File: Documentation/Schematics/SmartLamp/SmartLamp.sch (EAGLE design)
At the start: 34 parts, among them J1 POWER_JACKPTH_BREAD, Q1 STN4NF03L, Q2 STN4NF03L, Q3 STN4NF03L, U1 TPS71530, U2 DS3231MZ, U3 ATMEGA8/168/328MLF, U4 HM-10, X1 16MHz

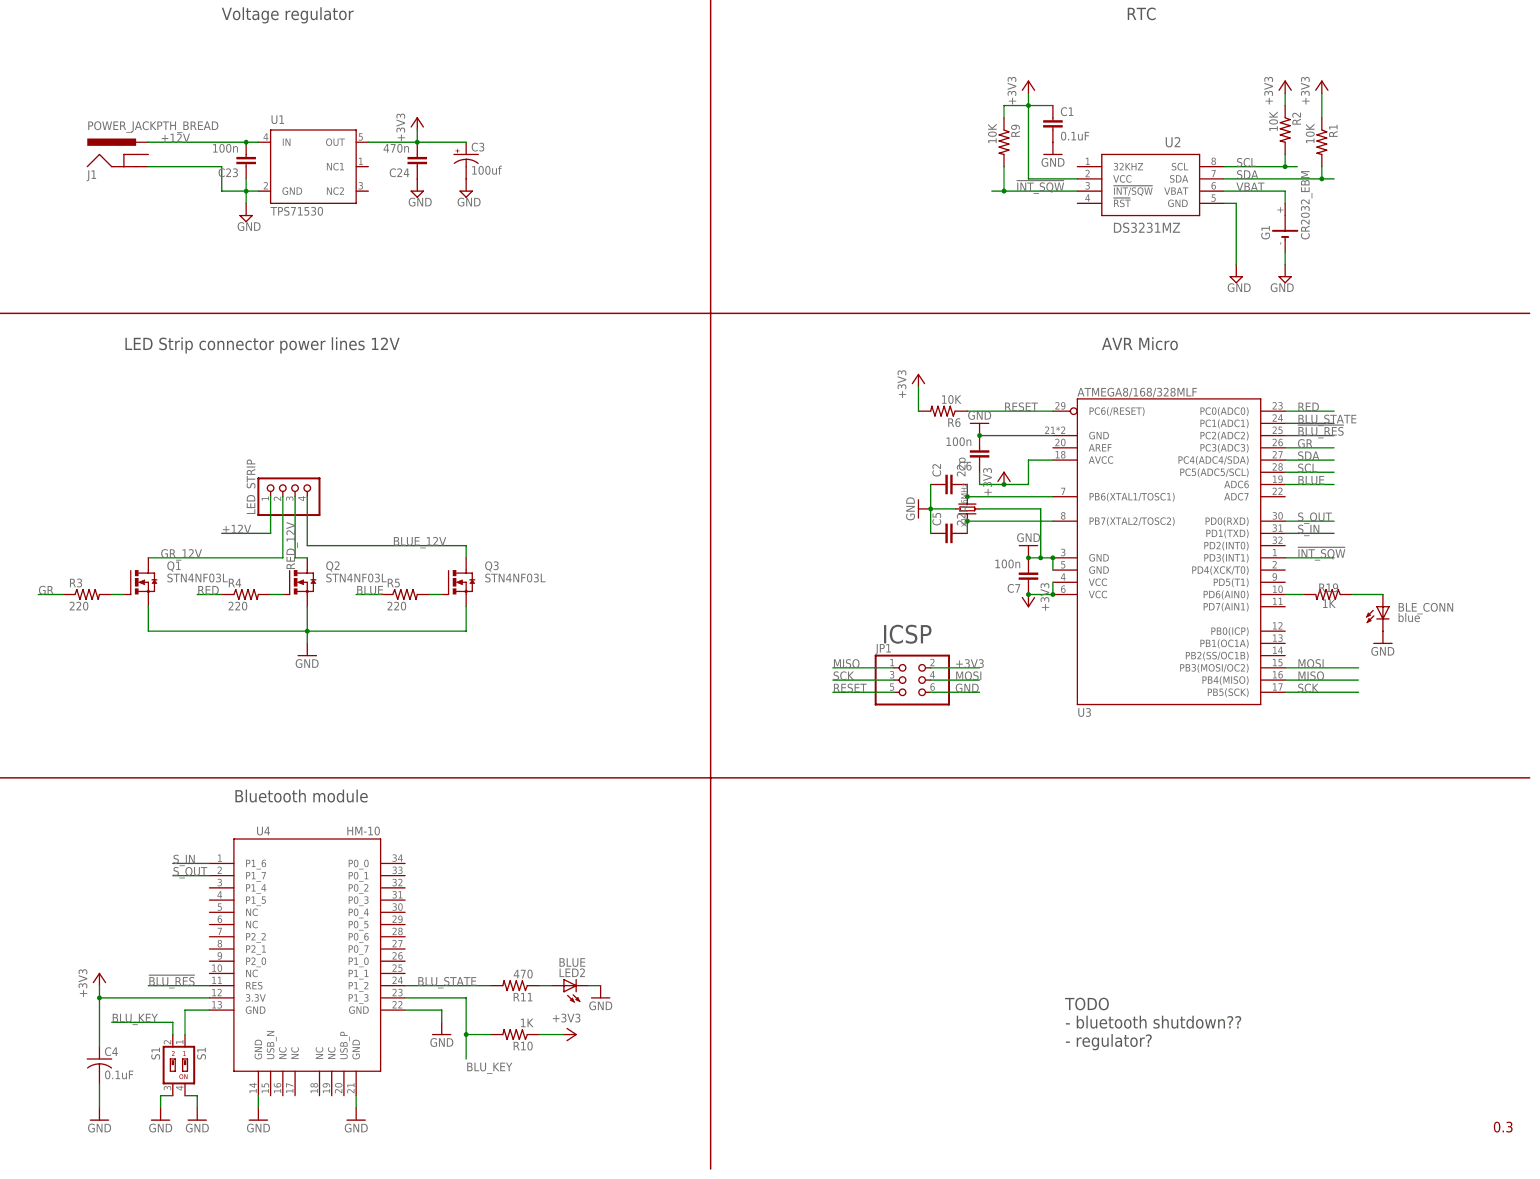
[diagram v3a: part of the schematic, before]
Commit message: Changed micro package, added IDC connector, replace regulatot. Some component to be checked
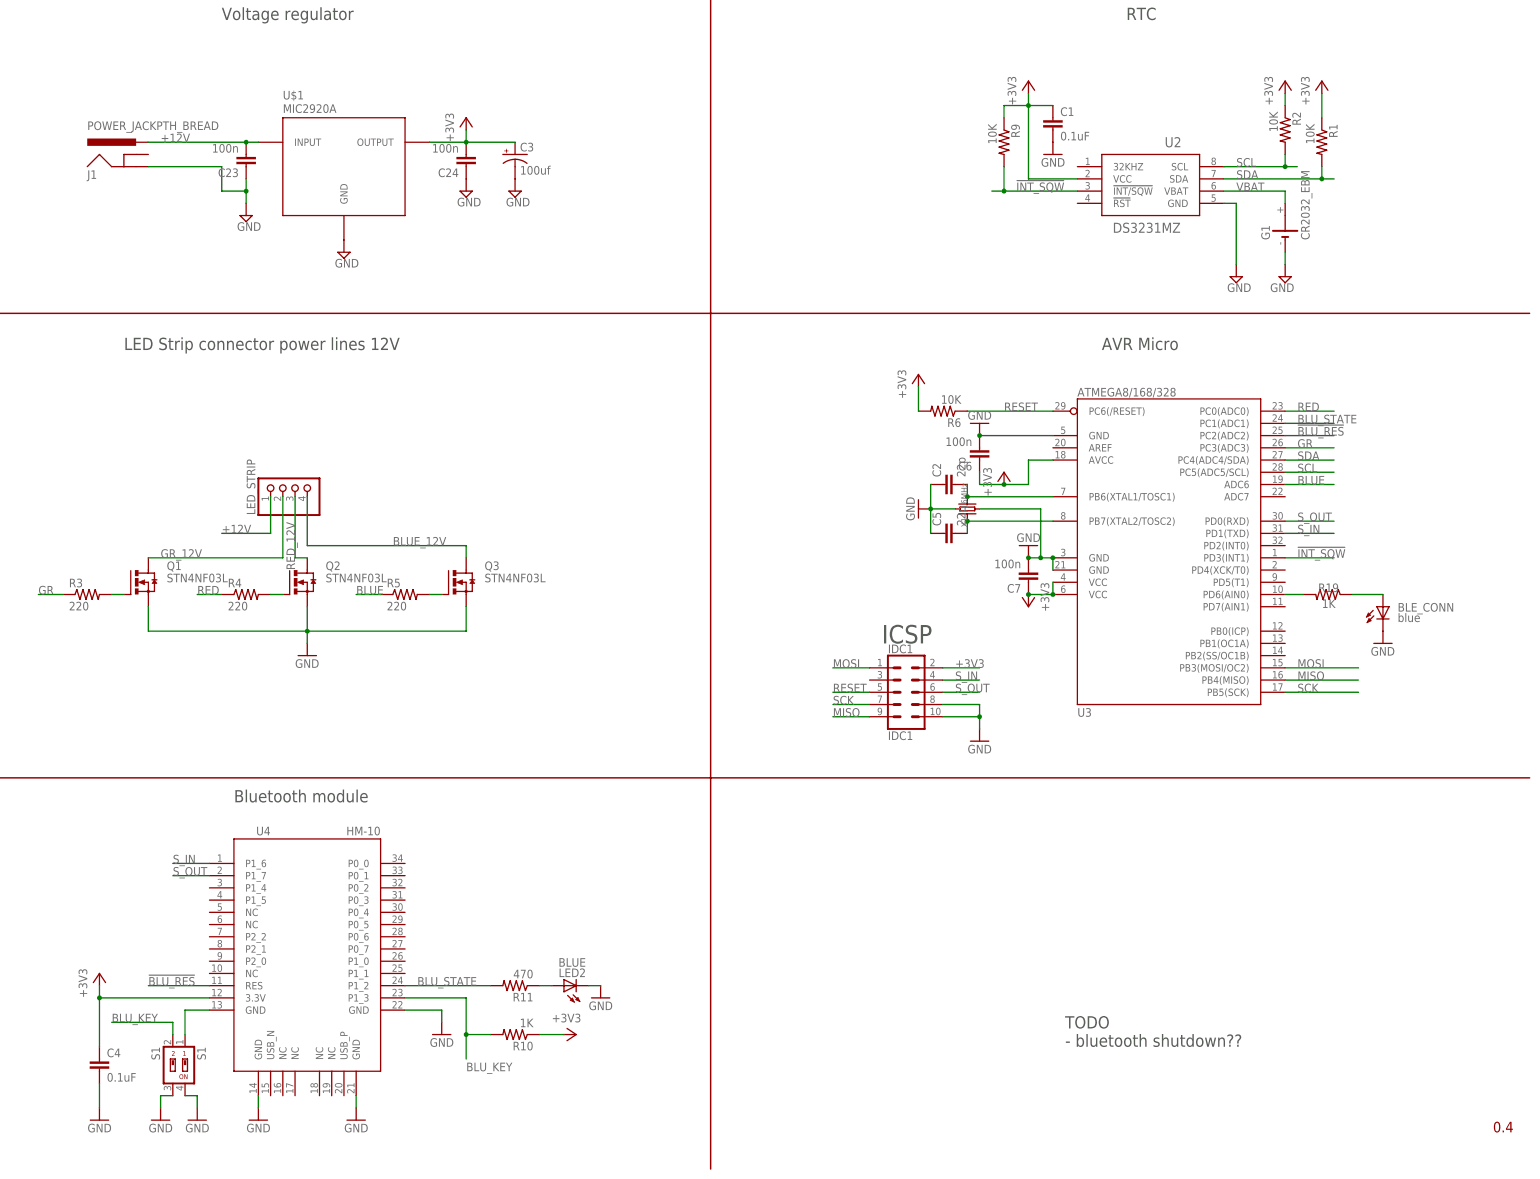
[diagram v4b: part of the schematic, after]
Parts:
- removed JP1: (no value), pinhead:PINHD-2X3
- removed U1: TPS71530, texas:TPS71530
- added IDC1: IDC1, SparkFun-Connectors:CONN_05X2SHD
- added U$1: MIC2920A, Microchip_LDO_regulator:MIC2920A
- C24: value 470n -> 100n
- C4: device adafruit:C-USC0805 -> rcl:C-EUC0805
- U3: value ATMEGA8/168/328MLF -> ATMEGA8/168/328; device IC:ATMEGA8/168/328MLF -> IC:ATMEGA8/168/328
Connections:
- net +12V: now also U$1.INPUT; no longer U1.IN
- net +3V3: now also IDC1.2, U$1.OUTPUT; no longer JP1.2, U1.OUT
- net GND: now also IDC1.10, IDC1.8, U$1.GND; no longer JP1.6, U1.GND
- net MISO: now also IDC1.9; no longer JP1.1
- net MOSI: now also IDC1.1; no longer JP1.4
- net RESET: now also IDC1.5; no longer JP1.5
- net SCK: now also IDC1.7; no longer JP1.3
- net S_IN: now also IDC1.4
- net S_OUT: now also IDC1.6
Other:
- note added: "TODO - bluetooth shutdown??"
- note removed: "TODO - bluetooth shutdown?? - regulator?"
- moved on the sheet: C24, C3, U3
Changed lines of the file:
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@@
 <schematic xreflabel="%F%N/%S" xrefpart="/%S.%C%R">
 <attributes>
-<attribute name="VERSION" value="0.3"/>
+<attribute name="VERSION" value="0.4"/>
 </attributes>
 <variantdefs>
@@
 <class number="0" name="default" width="0" drill="0">
 </class>
-<class number="1" name="12V" width="0.508" drill="0.254">
+<class number="1" name="12V" width="0.381" drill="0.254">
 <clearance class="1" value="0.2032"/>
 </class>
@@
 <part name="SUPPLY52" library="supply2" deviceset="GND" device=""/>
 <part name="C23" library="rcl" deviceset="C-EU" device="C0805" value="100n"/>
-<part name="C24" library="rcl" deviceset="C-EU" device="C0805" value="470n"/>
+<part name="C24" library="rcl" deviceset="C-EU" device="C0805" value="100n"/>
 <part name="SUPPLY54" library="supply2" deviceset="GND" device=""/>
 <part name="SUPPLY55" library="supply1" deviceset="+3V3" device=""/>
-<part name="U1" library="texas" deviceset="TPS71530" device=""/>
 <part name="SUPPLY7" library="supply2" deviceset="GND" device=""/>
 <part name="GND10" library="supply1" deviceset="GND" device=""/>
@@
 <part name="C3" library="SparkFun-Capacitors" deviceset="CAP_POL" device="C" value="100uf"/>
 <part name="SUPPLY8" library="supply2" deviceset="GND" device=""/>
-<part name="U3" library="IC" deviceset="ATMEGA8/168/328" device="MLF"/>
+<part name="U3" library="IC" deviceset="ATMEGA8/168/328" device="" value="ATMEGA8/168/328"/>
 <part name="SUPPLY20" library="supply1" deviceset="GND" device=""/>
 <part name="SUPPLY19" library="supply1" deviceset="GND" device=""/>
@@
 <part name="GND11" library="supply1" deviceset="GND" device=""/>
 <part name="GND1" library="supply1" deviceset="GND" device=""/>
-<part name="C4" library="adafruit" deviceset="C-US" device="C0805" value="0.1uF"/>
+<part name="C4" library="rcl" deviceset="C-EU" device="C0805" value="0.1uF"/>
 <part name="+3V5" library="supply1" deviceset="+3V3" device=""/>
 <part name="+3V7" library="supply1" deviceset="+3V3" device=""/>
@@
 <part name="C6" library="rcl" deviceset="C-EU" device="C0805" value="100n"/>
 <part name="C7" library="rcl" deviceset="C-EU" device="C0805" value="100n"/>
-<part name="JP1" library="pinhead" deviceset="PINHD-2X3" device=""/>
+<part name="U$1" library="Microchip_LDO_regulator" deviceset="MIC2920A" device=""/>
+<part name="SUPPLY1" library="supply2" deviceset="GND" device=""/>
+<part name="IDC1" library="SparkFun-Connectors" deviceset="CONN_05X2" device="SHD" value="IDC1"/>
+<part name="GND14" library="supply1" deviceset="GND" device=""/>
 </parts>
 <sheets>
@@
 <text x="337.82" y="175.26" size="2.54" layer="97" font="vector" ratio="16">AVR Micro</text>
 <text x="330.2" y="30.48" size="2.54" layer="97" font="vector">TODO
-- bluetooth shutdown??
-- regulator?</text>
+- bluetooth shutdown??</text>
 <wire x1="81.28" y1="86.36" x2="256.54" y2="86.36" width="0.3048" layer="94"/>
 <wire x1="256.54" y1="86.36" x2="426.72" y2="86.36" width="0.3048" layer="94"/>
@@
 <instance part="SUPPLY52" gate="GND" x="160.02" y="203.2"/>
 <instance part="C23" gate="G$1" x="160.02" y="213.36" rot="R180"/>
-<instance part="C24" gate="G$1" x="195.58" y="213.36" rot="R180"/>
-<instance part="SUPPLY54" gate="GND" x="195.58" y="208.28"/>
-<instance part="SUPPLY55" gate="G$1" x="195.58" y="223.52"/>
-<instance part="U1" gate="G$1" x="172.72" y="213.36"/>
+<instance part="C24" gate="G$1" x="205.74" y="213.36" rot="R180"/>
+<instance part="SUPPLY54" gate="GND" x="205.74" y="208.28"/>
+<instance part="SUPPLY55" gate="G$1" x="205.74" y="223.52"/>
 <instance part="SUPPLY7" gate="GND" x="365.76" y="190.5"/>
 <instance part="GND10" gate="1" x="172.72" y="111.76"/>
@@
 <instance part="R6" gate="G$1" x="304.8" y="162.56" rot="R180"/>
 <instance part="+3V1" gate="G$1" x="299.72" y="170.18"/>
-<instance part="C3" gate="G$1" x="205.74" y="215.9"/>
-<instance part="SUPPLY8" gate="GND" x="205.74" y="208.28"/>
+<instance part="C3" gate="G$1" x="215.9" y="215.9"/>
+<instance part="SUPPLY8" gate="GND" x="215.9" y="208.28"/>
 <instance part="U3" gate="G$1" x="350.52" y="137.16"/>
 <instance part="SUPPLY20" gate="1" x="312.42" y="160.02" rot="R180"/>
@@
 <instance part="C6" gate="G$1" x="312.42" y="152.4" rot="R180"/>
 <instance part="C7" gate="G$1" x="322.58" y="127" rot="R180"/>
-<instance part="JP1" gate="A" x="297.18" y="106.68"/>
+<instance part="U$1" gate="G$1" x="180.34" y="213.36"/>
+<instance part="SUPPLY1" gate="GND" x="180.34" y="195.58"/>
+<instance part="IDC1" gate="G$1" x="297.18" y="104.14"/>
+<instance part="GND14" gate="1" x="312.42" y="93.98" rot="MR0"/>
 </instances>
 <busses>
 </busses>
 <nets>
-<net name="GND" class="0">
+<net name="GND" class="1">
 <segment>
 <pinref part="GND4" gate="1" pin="GND"/>
@@
 </segment>
 <segment>
-<pinref part="U1" gate="G$1" pin="GND"/>
 <pinref part="SUPPLY52" gate="GND" pin="GND"/>
-<wire x1="162.56" y1="208.28" x2="160.02" y2="208.28" width="0.1524" layer="91"/>
 <wire x1="160.02" y1="208.28" x2="160.02" y2="205.74" width="0.1524" layer="91"/>
 <pinref part="C23" gate="G$1" pin="1"/>
@@
 </segment>
 <segment>
-<pinref part="JP1" gate="A" pin="6"/>
-<wire x1="302.26" y1="104.14" x2="312.42" y2="104.14" width="0.1524" layer="91"/>
-<label x="307.34" y="104.14" size="1.778" layer="95" font="vector"/>
+<pinref part="U$1" gate="G$1" pin="GND"/>
+<pinref part="SUPPLY1" gate="GND" pin="GND"/>
+</segment>
+<segment>
+<pinref part="IDC1" gate="G$1" pin="8"/>
+<wire x1="304.8" y1="101.6" x2="312.42" y2="101.6" width="0.1524" layer="91"/>
+<pinref part="IDC1" gate="G$1" pin="10"/>
+<wire x1="304.8" y1="99.06" x2="312.42" y2="99.06" width="0.1524" layer="91"/>
+<wire x1="312.42" y1="99.06" x2="312.42" y2="101.6" width="0.1524" layer="91"/>
+<pinref part="GND14" gate="1" pin="GND"/>
+<wire x1="312.42" y1="99.06" x2="312.42" y2="96.52" width="0.1524" layer="91"/>
+<junction x="312.42" y="99.06"/>
 </segment>
 </net>
@@
 </segment>
 <segment>
-<pinref part="JP1" gate="A" pin="5"/>
-<wire x1="294.64" y1="104.14" x2="281.94" y2="104.14" width="0.1524" layer="91"/>
+<pinref part="IDC1" gate="G$1" pin="5"/>
+<wire x1="289.56" y1="104.14" x2="281.94" y2="104.14" width="0.1524" layer="91"/>
 <label x="281.94" y="104.14" size="1.778" layer="95" font="vector"/>
 </segment>
@@
 <pinref part="C24" gate="G$1" pin="2"/>
 <pinref part="SUPPLY55" gate="G$1" pin="+3V3"/>
-<wire x1="195.58" y1="220.98" x2="195.58" y2="218.44" width="0.1524" layer="91"/>
-<pinref part="U1" gate="G$1" pin="OUT"/>
-<wire x1="185.42" y1="218.44" x2="195.58" y2="218.44" width="0.1524" layer="91"/>
-<junction x="195.58" y="218.44"/>
+<wire x1="205.74" y1="220.98" x2="205.74" y2="218.44" width="0.1524" layer="91"/>
+<pinref part="U$1" gate="G$1" pin="OUTPUT"/>
+<wire x1="198.12" y1="218.44" x2="205.74" y2="218.44" width="0.1524" layer="91"/>
+<junction x="205.74" y="218.44"/>
 <pinref part="C3" gate="G$1" pin="+"/>
-<wire x1="195.58" y1="218.44" x2="205.74" y2="218.44" width="0.1524" layer="91"/>
+<wire x1="205.74" y1="218.44" x2="215.9" y2="218.44" width="0.1524" layer="91"/>
 </segment>
 <segment>
@@
 </segment>
 <segment>
-<pinref part="JP1" gate="A" pin="2"/>
-<wire x1="302.26" y1="109.22" x2="312.42" y2="109.22" width="0.1524" layer="91"/>
+<pinref part="IDC1" gate="G$1" pin="2"/>
+<wire x1="304.8" y1="109.22" x2="312.42" y2="109.22" width="0.1524" layer="91"/>
 <label x="307.34" y="109.22" size="1.778" layer="95" font="vector"/>
 </segment>
@@
 <segment>
 <pinref part="J1" gate="G$1" pin="PWR"/>
-<pinref part="U1" gate="G$1" pin="IN"/>
 <wire x1="139.7" y1="218.44" x2="160.02" y2="218.44" width="0.1524" layer="91"/>
 <label x="142.24" y="218.44" size="1.778" layer="95" font="vector"/>
@@
 <wire x1="160.02" y1="218.44" x2="162.56" y2="218.44" width="0.1524" layer="91"/>
 <junction x="160.02" y="218.44"/>
+<pinref part="U$1" gate="G$1" pin="INPUT"/>
 </segment>
 </net>
@@
 <label x="378.46" y="139.7" size="1.778" layer="95" font="vector"/>
 </segment>
+<segment>
+<pinref part="IDC1" gate="G$1" pin="6"/>
+<wire x1="304.8" y1="104.14" x2="312.42" y2="104.14" width="0.1524" layer="91"/>
+<label x="307.34" y="104.14" size="1.778" layer="95" font="vector"/>
+</segment>
 </net>
 <net name="SCK" class="0">
@@
 </segment>
 <segment>
-<pinref part="JP1" gate="A" pin="3"/>
-<wire x1="294.64" y1="106.68" x2="281.94" y2="106.68" width="0.1524" layer="91"/>
-<label x="281.94" y="106.68" size="1.778" layer="95" font="vector"/>
+<pinref part="IDC1" gate="G$1" pin="7"/>
+<wire x1="289.56" y1="101.6" x2="281.94" y2="101.6" width="0.1524" layer="91"/>
+<label x="281.94" y="101.6" size="1.778" layer="95" font="vector"/>
 </segment>
 </net>
@@
 </segment>
 <segment>
-<pinref part="JP1" gate="A" pin="4"/>
-<wire x1="302.26" y1="106.68" x2="312.42" y2="106.68" width="0.1524" layer="91"/>
-<label x="307.34" y="106.68" size="1.778" layer="95" font="vector"/>
+<pinref part="IDC1" gate="G$1" pin="1"/>
+<wire x1="289.56" y1="109.22" x2="281.94" y2="109.22" width="0.1524" layer="91"/>
+<label x="281.94" y="109.22" size="1.778" layer="95" font="vector"/>
 </segment>
 </net>
@@
 <label x="378.46" y="137.16" size="1.778" layer="95" font="vector"/>
 </segment>
+<segment>
+<pinref part="IDC1" gate="G$1" pin="4"/>
+<wire x1="304.8" y1="106.68" x2="312.42" y2="106.68" width="0.1524" layer="91"/>
+<label x="307.34" y="106.68" size="1.778" layer="95" font="vector"/>
+</segment>
 </net>
 <net name="N$1" class="0">
@@
 </segment>
 <segment>
-<pinref part="JP1" gate="A" pin="1"/>
-<wire x1="294.64" y1="109.22" x2="281.94" y2="109.22" width="0.1524" layer="91"/>
-<label x="281.94" y="109.22" size="1.778" layer="95" font="vector"/>
+<pinref part="IDC1" gate="G$1" pin="9"/>
+<wire x1="289.56" y1="99.06" x2="281.94" y2="99.06" width="0.1524" layer="91"/>
+<label x="281.94" y="99.06" size="1.778" layer="95" font="vector"/>
 </segment>
 </net>
@@
 </sheet>
 </sheets>
+<errors>
+</errors>
 </schematic>
 </drawing>
